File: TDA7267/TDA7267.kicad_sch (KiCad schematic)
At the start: 18 parts, among them U1 TDA7267

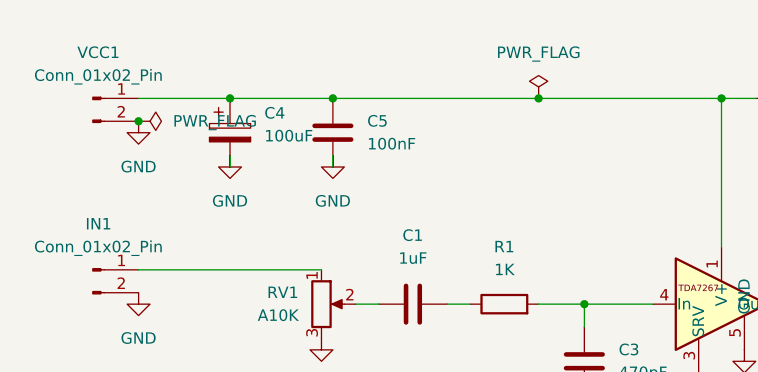
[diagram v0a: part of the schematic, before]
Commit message: Bottom GND plane
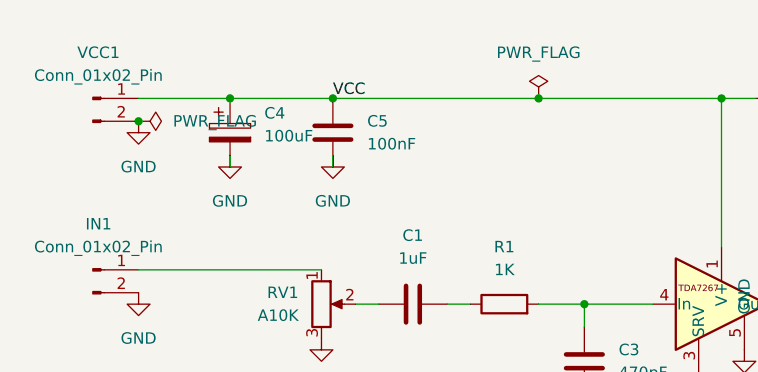
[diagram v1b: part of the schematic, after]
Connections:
- net VCC: now reaches C4.1, C5.2, R2.2, U1.1 (V+), VCC1.1 (Pin_1)
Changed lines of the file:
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@@
+		)
+	)
+	(label "VCC"
+		(at 77.47 63.5 0)
+		(effects
+			(font
+				(size 1.27 1.27)
+			)
+			(justify left bottom)
 		)
 	)
